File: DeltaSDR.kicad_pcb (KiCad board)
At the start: 2 copper layers, 100 x 80 mm, 178 parts, among them J1 Conn_01x03_Male, J2 Conn_01x05_Male, J3 Barrel_Jack, J4 USB_A, J5 Conn_Coaxial, J6 Conn_01x02_Male, Q1 BSS123, Q2 BSS123, Q3 BSS123, Q4 BSS123, Q5 BSS123, Q6 BSS123, Q7 MMBT3904, T1 Transformer_1P_SS, T2 Transformer_1P_SS, U1 MCP1703T-3302E/DB, U10 TLV2464CD, U11 SN74CBT3253, U12 MMG3H21NT1, U2 Si570, U3 SN74CBT3253, U4 PCM3060, U5 CY8C3246PVI-147, U6 MCP1703T-5002E/DB, U7 MCP1703T-5002E/DB, U8 74HC74, U9 LT6231CSB, Y1 Crystal_GND24

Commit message: Wrong TX resistors values correction.
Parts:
- R17, R20, R21, R23, R26, R30: value 49k9 -> 49R9
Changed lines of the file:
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@@
       (effects (font (size 1 1) (thickness 0.15)))
     )
-    (fp_text value 49k9 (at 0 1.43 90) (layer F.Fab)
+    (fp_text value 49R9 (at 0 1.43 90) (layer F.Fab)
       (effects (font (size 1 1) (thickness 0.15)))
     )
@@
       (effects (font (size 1 1) (thickness 0.15)))
     )
-    (fp_text value 49k9 (at 0 1.43 90) (layer F.Fab)
+    (fp_text value 49R9 (at 0 1.43 90) (layer F.Fab)
       (effects (font (size 1 1) (thickness 0.15)))
     )
@@
       (effects (font (size 1 1) (thickness 0.15)))
     )
-    (fp_text value 49k9 (at 0 1.43) (layer F.Fab)
+    (fp_text value 49R9 (at 0 1.43) (layer F.Fab)
       (effects (font (size 1 1) (thickness 0.15)))
     )
@@
       (effects (font (size 1 1) (thickness 0.15)))
     )
-    (fp_text value 49k9 (at 0 1.43) (layer F.Fab)
+    (fp_text value 49R9 (at 0 1.43) (layer F.Fab)
       (effects (font (size 1 1) (thickness 0.15)))
     )
@@
       (effects (font (size 1 1) (thickness 0.15)))
     )
-    (fp_text value 49k9 (at 0 1.43) (layer F.Fab)
+    (fp_text value 49R9 (at 0 1.43) (layer F.Fab)
       (effects (font (size 1 1) (thickness 0.15)))
     )
@@
       (effects (font (size 1 1) (thickness 0.15)))
     )
-    (fp_text value 49k9 (at 0 1.43) (layer F.Fab)
-      (effects (font (size 1 1) (thickness 0.15)))
-    )
+    (fp_text value 49R9 (at 0 1.43) (layer F.Fab)
+      (effects (font (size 1 1) (thickness 0.15)))
+    )

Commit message: Corrected wrong TX opamp capacitors values
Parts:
- C37, C41, C47, C50: value 100n -> 100p
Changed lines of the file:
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@@
       (effects (font (size 1 1) (thickness 0.15)))
     )
-    (fp_text value 100n (at 0 1.43 90) (layer F.Fab)
+    (fp_text value 100p (at 0 1.43 90) (layer F.Fab)
       (effects (font (size 1 1) (thickness 0.15)))
     )
@@
       (effects (font (size 1 1) (thickness 0.15)))
     )
-    (fp_text value 100n (at 0 1.43 90) (layer F.Fab)
+    (fp_text value 100p (at 0 1.43 90) (layer F.Fab)
       (effects (font (size 1 1) (thickness 0.15)))
     )
@@
       (effects (font (size 1 1) (thickness 0.15)))
     )
-    (fp_text value 100n (at 0 1.43 90) (layer F.Fab)
+    (fp_text value 100p (at 0 1.43 90) (layer F.Fab)
       (effects (font (size 1 1) (thickness 0.15)))
     )
@@
       (effects (font (size 1 1) (thickness 0.15)))
     )
-    (fp_text value 100n (at 0 1.43 90) (layer F.Fab)
-      (effects (font (size 1 1) (thickness 0.15)))
-    )
+    (fp_text value 100p (at 0 1.43 90) (layer F.Fab)
+      (effects (font (size 1 1) (thickness 0.15)))
+    )

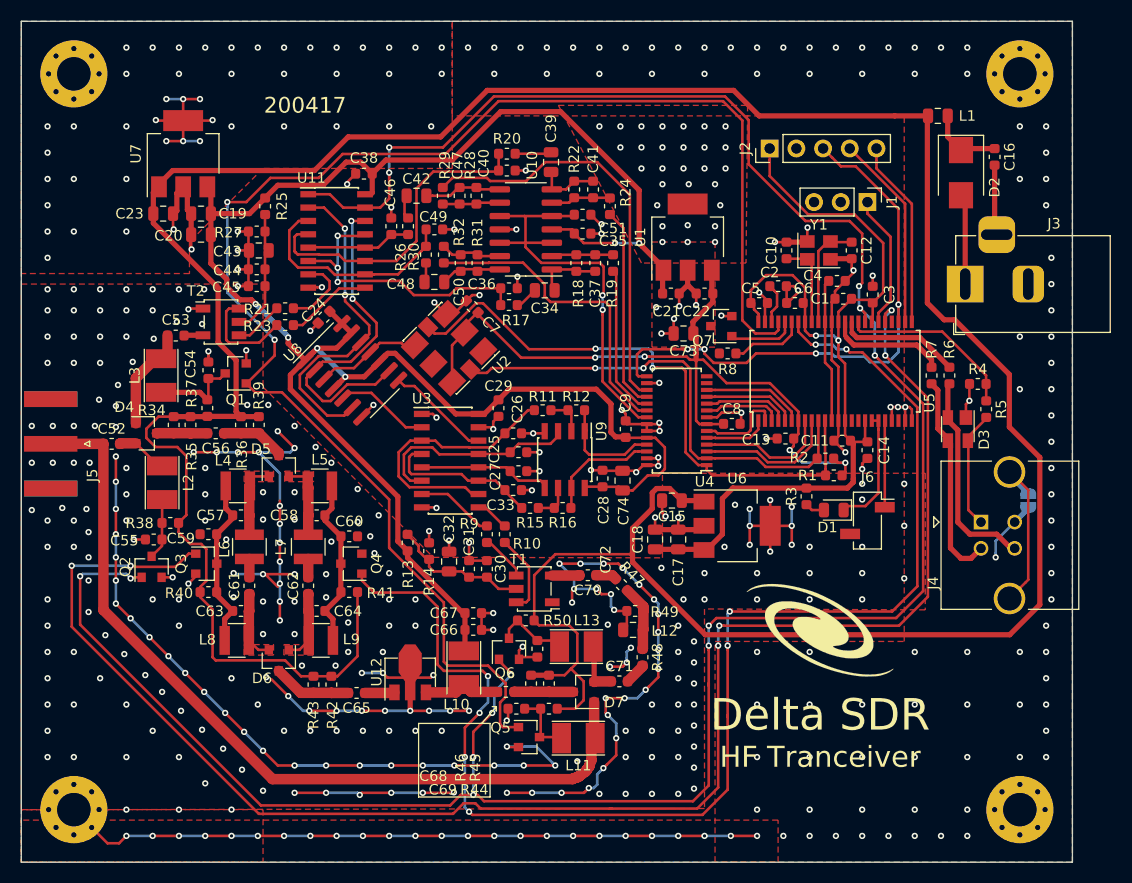
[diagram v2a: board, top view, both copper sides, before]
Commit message: TX opamp improved layout.
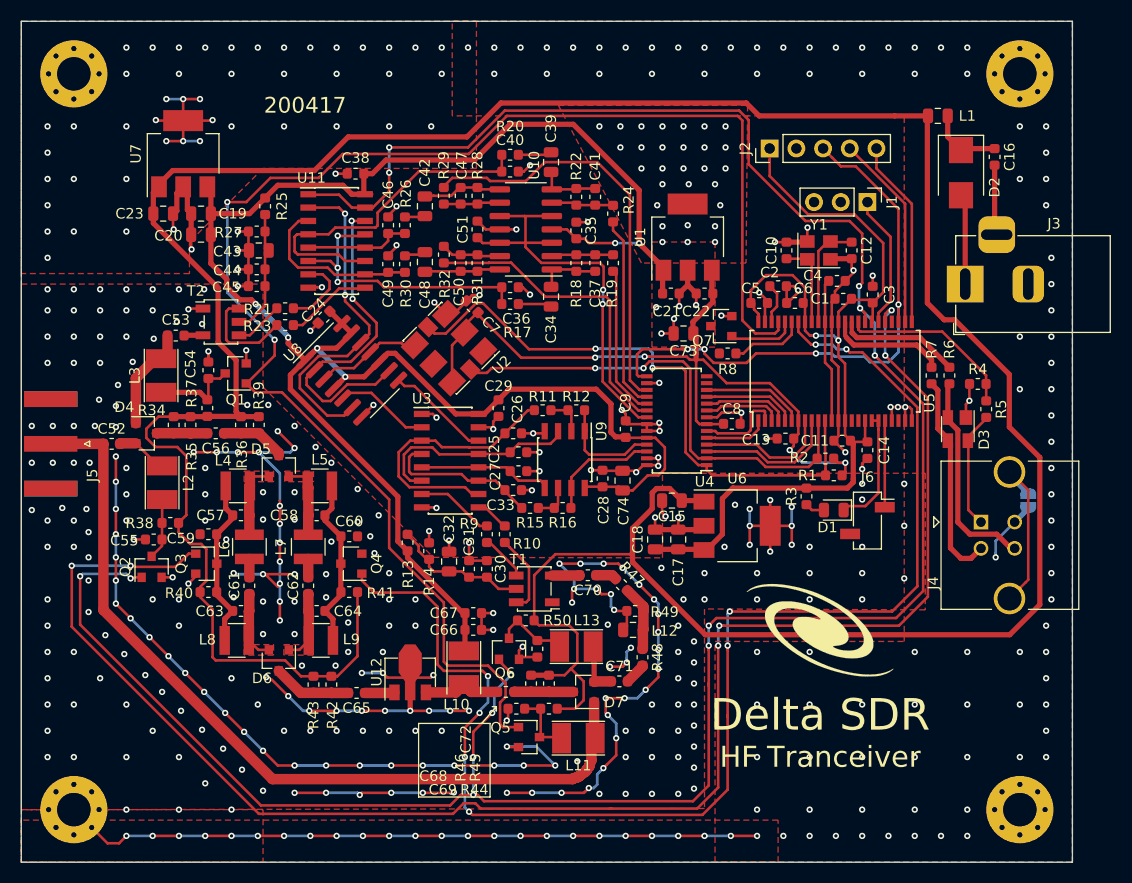
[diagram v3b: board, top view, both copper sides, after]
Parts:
- moved C51 10.1 mm to (153.4, 79.8), turned to 90 degrees
- moved C49 5.50 mm to (144.9, 83.1), turned to 90 degrees
- moved R30 2.19 mm to (146.5, 83.1), turned to 90 degrees
- moved C48 2.10 mm to (148.4, 82.9), turned to 270 degrees
- moved C42 1.28 mm to (148.4, 77.6), turned to 90 degrees
- moved C34 0.85 mm to (160.4, 86.2), turned to 90 degrees
- moved C38 0.80 mm to (141.8, 74.5)
- moved R24 0.76 mm to (166.3, 78.3)
- moved R22 0.73 mm to (162.8, 76.7)
- moved C41 0.73 mm to (164.6, 76.7)
- moved C35 0.67 mm to (162.8, 79.9), turned to 90 degrees
- moved R20 0.32 mm to (156.5, 72.7)
- moved C40 0.32 mm to (156.5, 74.3)
- moved R26 0.32 mm to (146.5, 79.4)
- moved C46 0.32 mm to (144.9, 79.4)
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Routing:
- net Net-(C49-Pad1): track 21.0 -> 16.5 mm
- net Net-(C40-Pad1): track 30.1 -> 32.3 mm
- net GND: track 483.1 -> 485.3 mm, vias 524 -> 523
- net HI_RX: track 238.0 -> 236.5 mm
- net +5V: track 190.6 -> 189.1 mm
- net Net-(C48-Pad2): track 5.72 -> 7.12 mm
- net HI_TX: track 146.3 -> 145.2 mm
- net +12V: track 304.3 -> 303.3 mm
- net Net-(C34-Pad1): track 2.25 -> 3.21 mm
- net QSE_J: track 31.7 -> 32.6 mm
- net VOUTR+: track 19.3 -> 18.4 mm
- net Net-(C46-Pad1): track 10.6 -> 11.3 mm
- net Net-(C42-Pad1): track 2.45 -> 1.83 mm

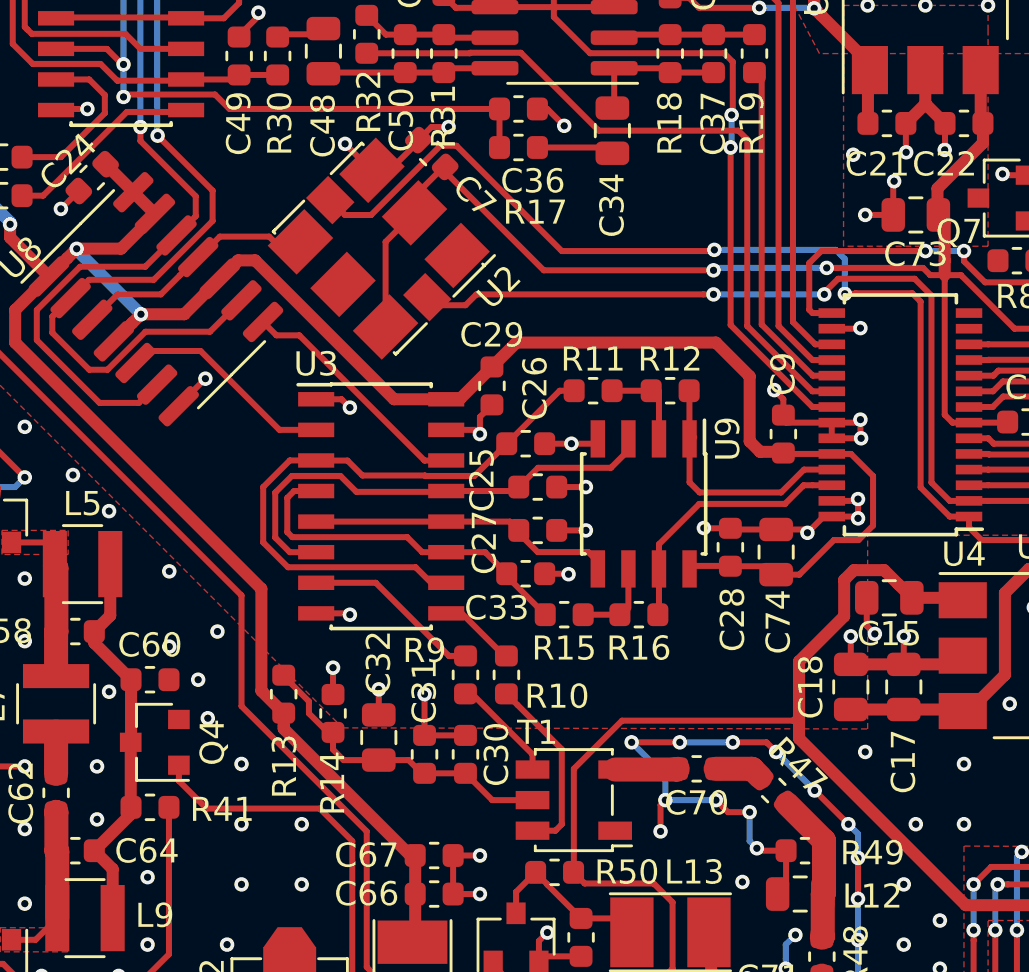
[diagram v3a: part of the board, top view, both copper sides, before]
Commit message: Added capacitors to codec's VCOM
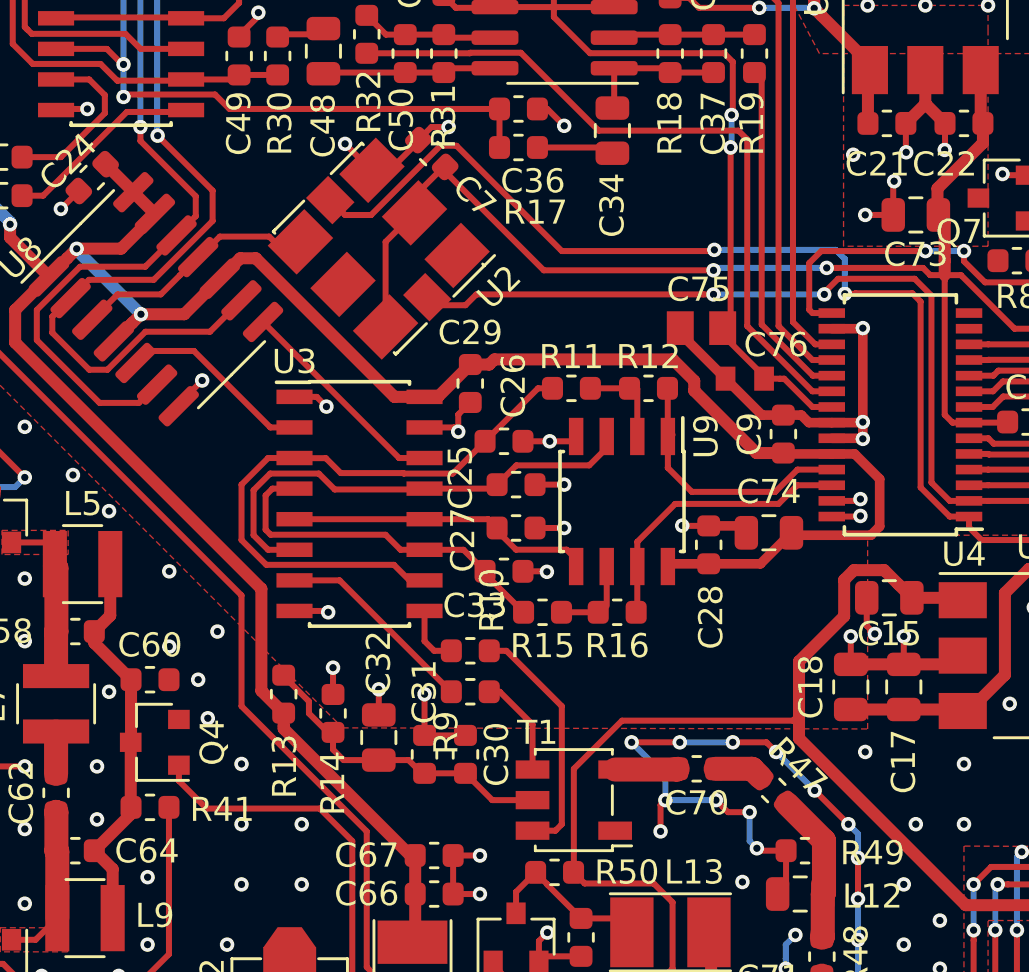
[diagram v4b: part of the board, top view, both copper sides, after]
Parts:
- added C75: 10u, Capacitor_SMD:C_0805_2012Metric, F.Cu at (164.1, 94.4)
- added C76: 100n, Capacitor_SMD:C_0603_1608Metric, F.Cu at (165.9, 96.5)
- R12, R16: value tbd -> 1k
- moved R10 1.80 mm to (154.5, 107.8), turned to 180 degrees
- moved C26 0.91 mm to (155.9, 99.1)
- moved C25 0.91 mm to (156.4, 100.9)
- moved C27 0.91 mm to (156.4, 102.7)
- moved C28 0.91 mm to (164.4, 103.4)
- moved C29 0.91 mm to (154.5, 96.7)
- moved C33 0.91 mm to (155.9, 104.5)
- moved R11 0.91 mm to (158.7, 96.9)
- moved R12 0.91 mm to (161.9, 96.9)
- moved R15 0.91 mm to (157.5, 106.2)
- moved R16 0.91 mm to (160.6, 106.2)
- moved U3 0.91 mm to (149.9, 101.7)
- moved U9 0.91 mm to (160.8, 101.6)
- moved C74 0.85 mm to (166.9, 102.9), turned to 180 degrees
- moved R9 0.73 mm to (154.5, 109.5), turned to 180 degrees
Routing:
- net GND: track 485.3 -> 489.5 mm, vias 523 -> 521
- net Net-(R10-Pad1): track 7.69 -> 10.2 mm
- net QSD_Q: track 10.5 -> 9.05 mm
- net +5V: track 189.1 -> 187.7 mm
- net Net-(R9-Pad2): track 8.36 -> 9.33 mm
- net VINR: track 11.3 -> 12.2 mm
- net VCOM: track 40.0 -> 40.8 mm
- net Net-(R10-Pad2): track 3.23 -> 2.53 mm
- net VINL: track 10.8 -> 11.4 mm
